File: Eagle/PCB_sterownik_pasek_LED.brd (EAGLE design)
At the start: 100 x 80 mm, 14 parts, among them IC3 NE555, Q1 IRF740

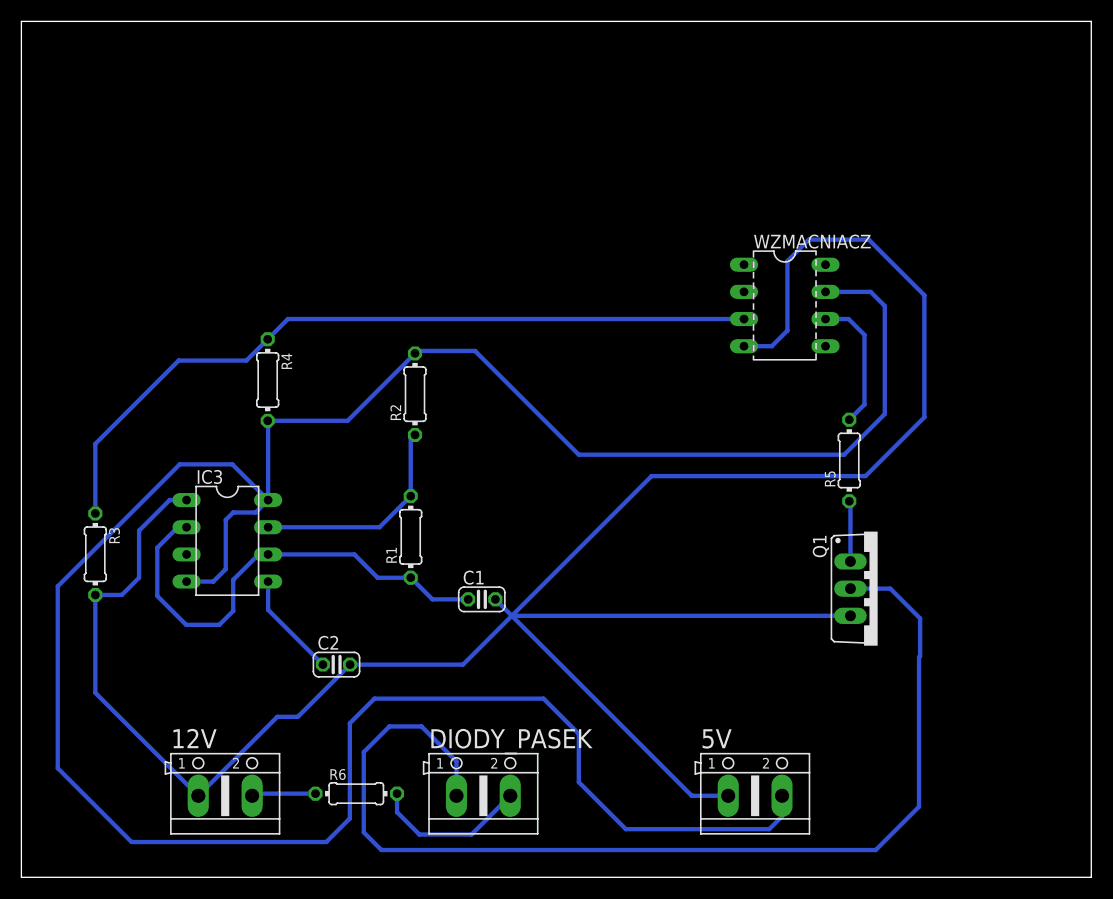
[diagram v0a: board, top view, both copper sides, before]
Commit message: zakończenie cz. elektronicznej.
Podłączenie na płytce stykowym pierwszych czujników + zamknięcie części sterownika do paska LED.
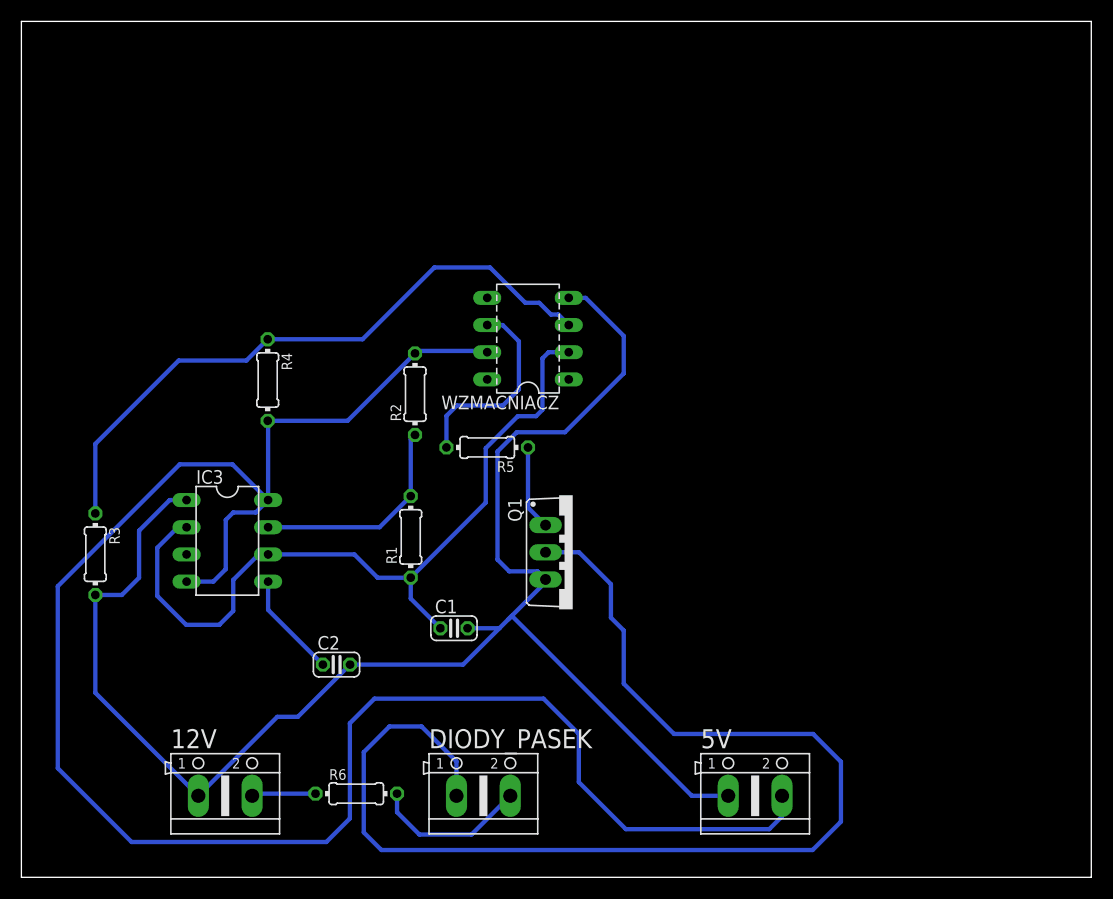
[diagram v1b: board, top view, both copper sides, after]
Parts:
- C1: value (none) -> 1u
- C2: value (none) -> 100n
- R1: value (none) -> 10k
- R2, R6: value (none) -> 1k
- R5: value (none) -> 100
- moved R5 33.9 mm to (43.5, 40.2), turned to 180 degrees
- moved Q1 28.7 mm to (51.5, 30.4)
- moved WZMACNIACZ 24.2 mm to (47.4, 50.4), turned to 90 degrees
- moved C1 3.75 mm to (40.4, 23.3)
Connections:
- removed net N$3: WZMACNIACZ.2
- net N$5: now also WZMACNIACZ.2
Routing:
- net GND: track 219.4 -> 149.5 mm
- net VCC: track 237.3 -> 178.4 mm
- net N$5: track 44.4 -> 73.3 mm
- net N$9: track 101.3 -> 114.2 mm
- net N$1: track 72.0 -> 59.8 mm
- net N$6: track 12.8 -> 18.8 mm
- net N$7: track 5.68 -> 7.94 mm
